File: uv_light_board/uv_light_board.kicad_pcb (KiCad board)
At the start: 2 copper layers, 78.7 x 49.5 mm, 14 parts, among them J1 Power, J2 Power

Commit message: Replacing the UV led with an SMD LED we can buy PnP
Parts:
- D1, D2, D3, D4, D5, D6: footprint LED_SMD:LED_1W_3W_R8 -> uv_lib:SMD3535-3P
- R1, R2: value 1R -> 6R
- moved D6 0.54 mm to (206.0, 81.8)
- moved D2 0.35 mm to (184.0, 108.9)
- moved D4 0.33 mm to (162.5, 81.6)
- moved D3 0.32 mm to (206.0, 109.4)
- moved D5 0.23 mm to (184.0, 81.1)
- moved D1 0.18 mm to (162.6, 109.4)
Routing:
- net Net-(D2-K): track 21.6 -> 25.8 mm
- net Net-(D5-K): track 21.6 -> 25.4 mm
- net Net-(D1-K): track 21.6 -> 24.7 mm
- net Net-(D4-K): track 21.6 -> 24.6 mm
- net Net-(D1-A): track 4.31 -> 6.89 mm
- net Net-(D4-A): track 9.86 -> 12.1 mm
- net +12V: track 85.2 -> 86.7 mm

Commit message: Adding more resistor choices to light PCB, tweaking LED footprint
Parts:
- added JP1: Jumper_2_Bridged, Jumper:SolderJumper-2_P1.3mm_Bridged2Bar_Pad1.0x1.5mm, F.Cu at (166.4, 105.6)
- added JP2: Jumper_2_Open, Jumper:SolderJumper-2_P1.3mm_Open_Pad1.0x1.5mm, F.Cu at (158.4, 74.3)
- added JP3: Jumper_2_Bridged, Jumper:SolderJumper-2_P1.3mm_Bridged2Bar_Pad1.0x1.5mm, F.Cu at (158.4, 77.0)
- added JP4: Jumper_2_Open, Jumper:SolderJumper-2_P1.3mm_Open_Pad1.0x1.5mm, F.Cu at (166.5, 100.9)
- added R3: 3R, Resistor_SMD:R_2512_6332Metric, F.Cu at (151.7, 83.6)
- added R4: 3R, Resistor_SMD:R_2512_6332Metric, F.Cu at (172.2, 100.7)
- moved R1 4.61 mm to (172.2, 105.6)
- moved R2 1.65 mm to (156.5, 83.5)
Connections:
- R1 pad 1: Net-(D1-A) -> Net-(JP1-B)
- R2 pad 1: Net-(D4-A) -> Net-(JP3-B)
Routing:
- net Net-(JP2-B): track 0.00 -> 10.6 mm
- net +12V: track 86.7 -> 94.5 mm
- net Net-(D1-A): track 6.89 -> 12.6 mm
- net Net-(JP3-B): track 0.00 -> 5.29 mm
- net Net-(JP4-B): track 0.00 -> 2.21 mm
- net Net-(JP1-B): track 0.00 -> 2.14 mm
- net Net-(D4-A): track 12.1 -> 10.1 mm

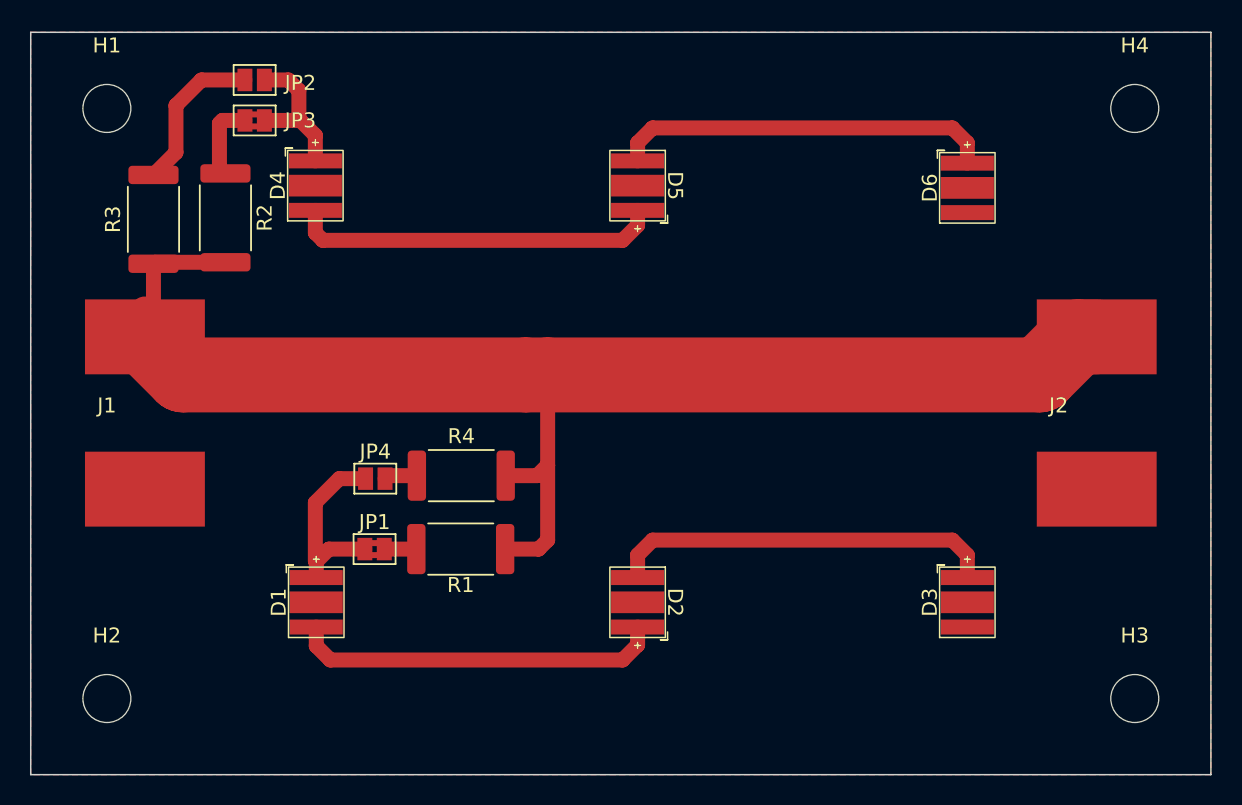
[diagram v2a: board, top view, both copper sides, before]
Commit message: Adding 3rd tuning resistor, fixing footprints on PCB
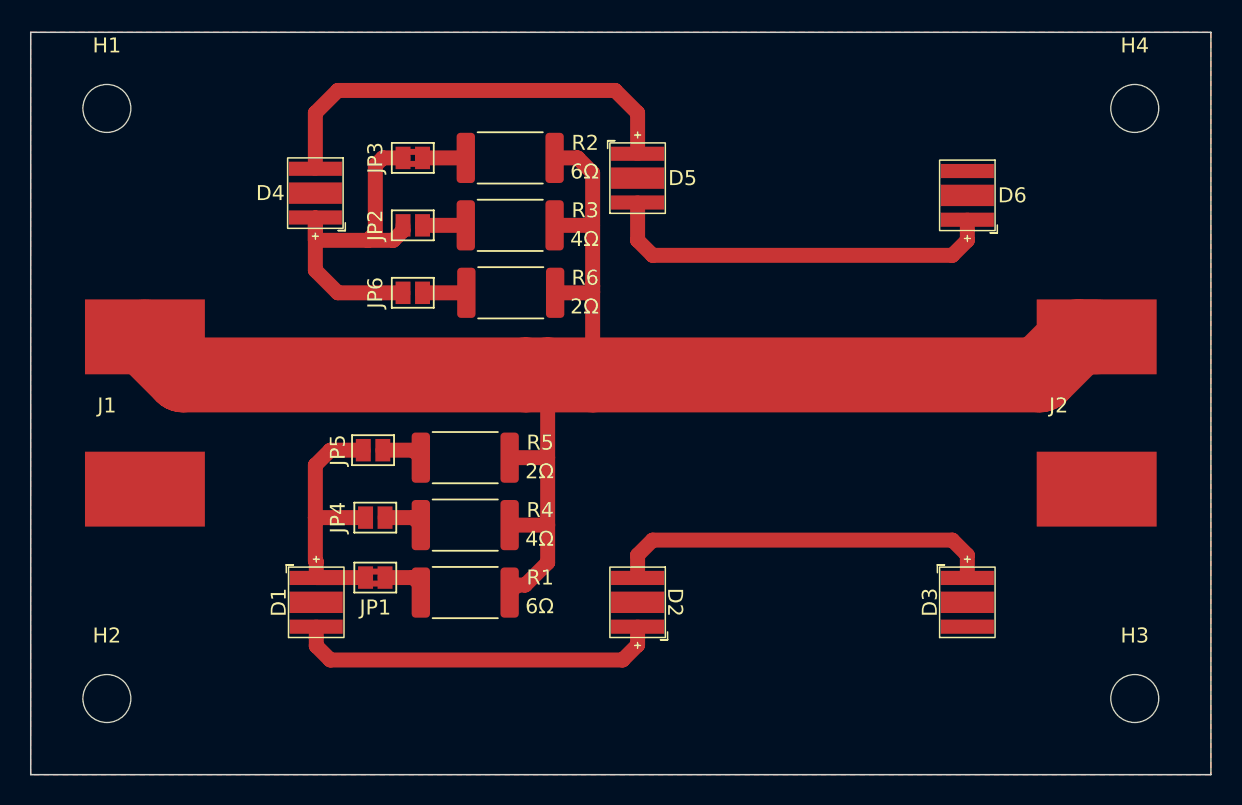
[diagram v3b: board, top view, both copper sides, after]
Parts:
- added JP5: Jumper_2_Open, Jumper:SolderJumper-2_P1.3mm_Open_Pad1.0x1.5mm, F.Cu at (166.3, 99.0)
- added JP6: Jumper_2_Open, Jumper:SolderJumper-2_P1.3mm_Open_Pad1.0x1.5mm, F.Cu at (169.0, 88.5)
- added R5: 2R, Resistor_SMD:R_2512_6332Metric, F.Cu at (172.5, 99.5)
- added R6: 2R, Resistor_SMD:R_2512_6332Metric, F.Cu at (175.5, 88.5)
- R3, R4: value 3R -> 4R
- moved R3 23.8 mm to (175.5, 84.0), turned to 0 degrees
- moved R2 19.4 mm to (175.5, 79.5), turned to 0 degrees
- moved JP2 14.3 mm to (169.0, 84.0), turned to 0 degrees
- moved JP3 10.8 mm to (169.0, 79.5), turned to 0 degrees
- moved R4 3.31 mm to (172.5, 104.0)
- moved R1 2.92 mm to (172.5, 108.5)
- moved JP4 2.60 mm to (166.5, 103.5)
- moved JP1 1.90 mm to (166.5, 107.5)
- turned D4 to -90 degrees
- turned D5 to 90 degrees
- turned D6 to -90 degrees
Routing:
- net Net-(D4-A): track 10.1 -> 25.2 mm
- net +12V: track 94.5 -> 109.3 mm
- net Net-(JP2-B): track 10.6 -> 2.89 mm
- net Net-(D1-A): track 12.6 -> 17.8 mm
- net Net-(D4-K): track 24.6 -> 29.1 mm
- net Net-(JP6-B): track 0.00 -> 2.92 mm
- net Net-(JP5-B): track 0.00 -> 2.74 mm
- net Net-(JP3-B): track 5.29 -> 2.89 mm
- net Net-(D5-K): track 25.4 -> 26.7 mm
- net Net-(JP1-B): track 2.14 -> 3.09 mm
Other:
- board text added: "2Ω"
- board text added: "4Ω"
- board text added: "6Ω"
